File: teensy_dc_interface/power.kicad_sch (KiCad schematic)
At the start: 51 parts, among them U3 AP65211A, U4 AP62200TWU-7, U9 AP65211A

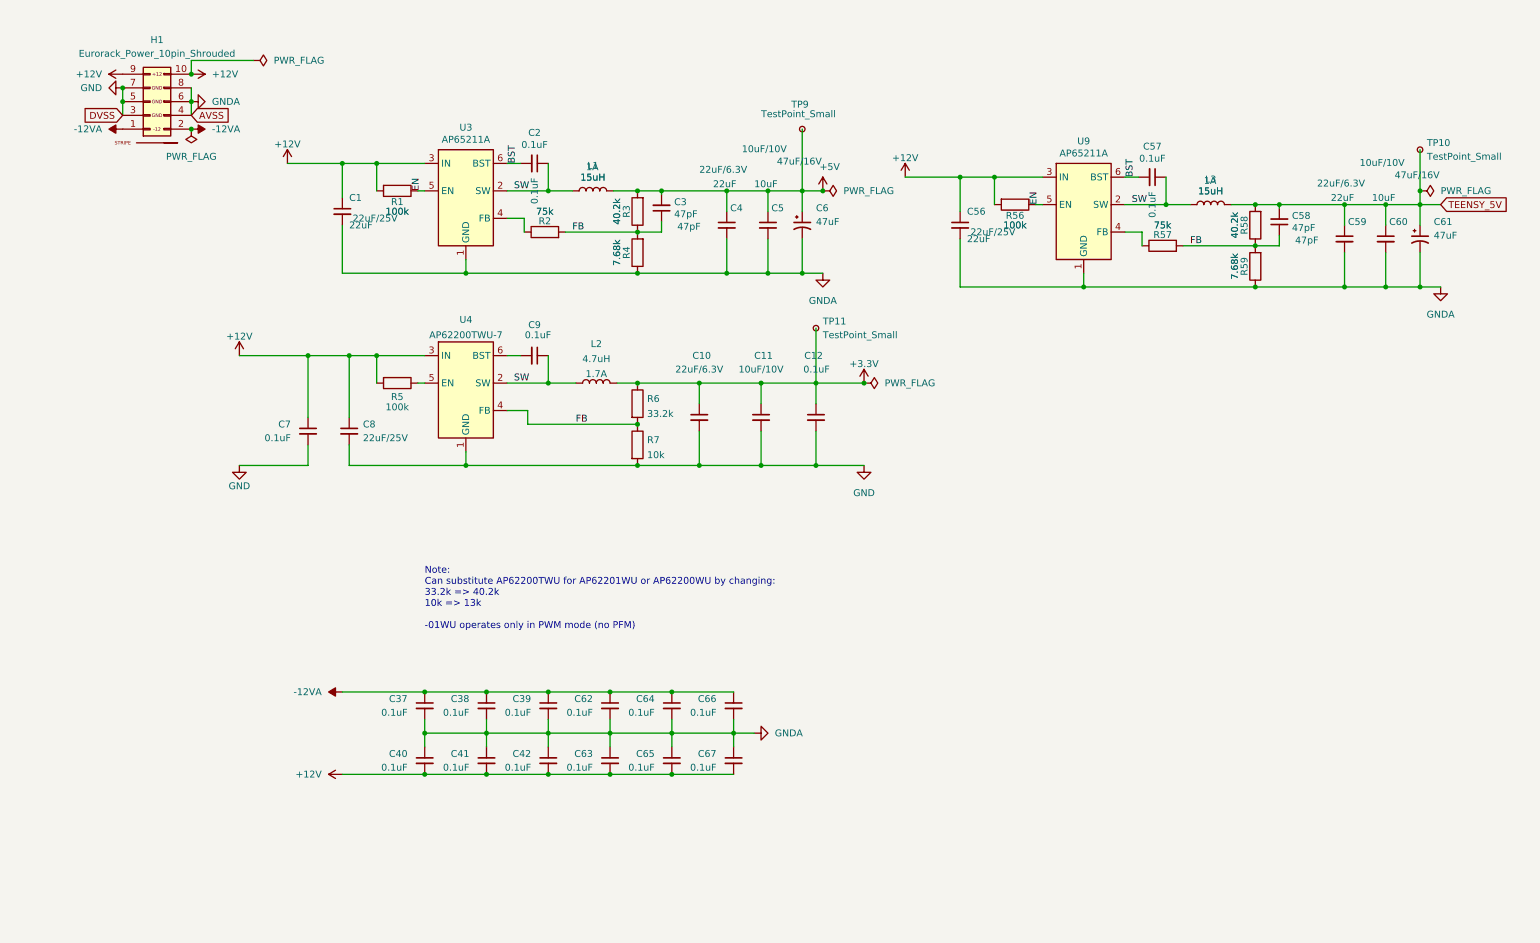
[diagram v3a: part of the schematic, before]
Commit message: Added layout for power regulators
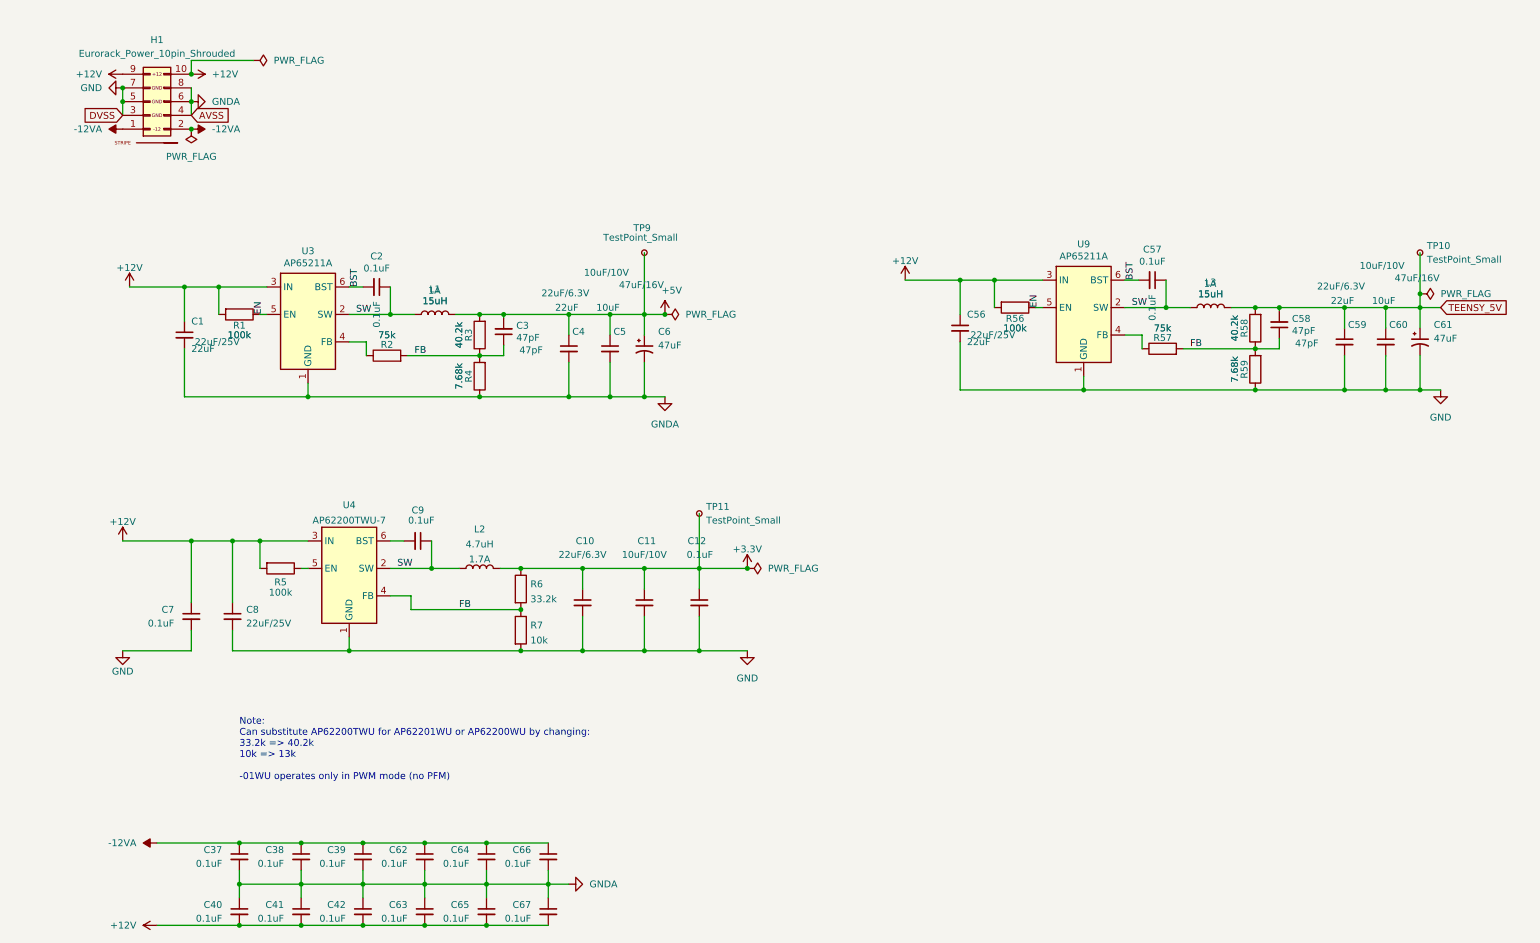
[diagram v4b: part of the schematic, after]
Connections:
- net GND: now also C56.2, C59.2, C60.2, C61.2, R59.1, U9.1 (GND)
- net GNDA: no longer C56.2, C59.2, C60.2, C61.2, R59.1, U9.1 (GND)
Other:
- moved on the sheet: C1, C10, C11, C12, C2, C3, C37, C38, C39, C4, C40, C41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

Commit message: Finished core electrical layout
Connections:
- net SW: no longer C2.1, C57.1, L1.1, L3.1, U3.2 (SW), U9.2 (SW)
- net BST: no longer names the net of C57.2, U9.6 (BST)
- net BST: no longer C2.2, U3.6 (BST)
- net EN: no longer names the net of R1.1, U3.5 (EN)
- net EN: no longer R56.1, U9.5 (EN)
- removed net FB: C3.1, C58.1, R2.2, R3.1, R4.2, R57.2, R58.1, R59.2, R6.2, R7.1, U4.4 (FB)
- new net: R6.2, R7.1, U4.4 (FB)
- new net: C57.1, L3.1, U9.2 (SW)
- new net: C3.1, R2.2, R3.1, R4.2
- new net: R56.1, U9.5 (EN)
- new net: C2.1, L1.1, U3.2 (SW)
- new net: C2.2, U3.6 (BST)
- new net: C58.1, R57.2, R58.1, R59.2
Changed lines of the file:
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@@
-	)
-	(label "SW"
-		(at 68.58 72.39 0)
-		(fields_autoplaced yes)
-		(effects
-			(font
-				(size 1.27 1.27)
-			)
-			(justify left bottom)
-		)
 	)
 	(label "SW"
@@
 		(fields_autoplaced yes)
 		(effects
-			(font
-				(size 1.27 1.27)
-			)
-			(justify left bottom)
-		)
-	)
-	(label "SW"
-		(at 212.09 71.12 0)
-		(fields_autoplaced yes)
-		(effects
-			(font
-				(size 1.27 1.27)
-			)
-			(justify left bottom)
-		)
-	)
-	(label "FB"
-		(at 79.375 80.01 0)
-		(fields_autoplaced yes)
-		(effects
-			(font
-				(size 1.27 1.27)
-			)
-			(justify left bottom)
-		)
-	)
-	(label "BST"
-		(at 212.725 66.04 90)
-		(fields_autoplaced yes)
-		(effects
-			(font
-				(size 1.27 1.27)
-			)
-			(justify left bottom)
-		)
-	)
-	(label "FB"
-		(at 222.885 78.74 0)
-		(fields_autoplaced yes)
-		(effects
-			(font
-				(size 1.27 1.27)
-			)
-			(justify left bottom)
-		)
-	)
-	(label "BST"
-		(at 69.215 67.31 90)
-		(fields_autoplaced yes)
-		(effects
-			(font
-				(size 1.27 1.27)
-			)
-			(justify left bottom)
-		)
-	)
-	(label "FB"
-		(at 87.63 127 0)
-		(fields_autoplaced yes)
-		(effects
-			(font
-				(size 1.27 1.27)
-			)
-			(justify left bottom)
-		)
-	)
-	(label "EN"
-		(at 194.945 71.12 90)
-		(fields_autoplaced yes)
-		(effects
-			(font
-				(size 1.27 1.27)
-			)
-			(justify left bottom)
-		)
-	)
-	(label "EN"
-		(at 51.435 72.39 90)
-		(fields_autoplaced yes)
-		(effects

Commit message: sizing, remove SW label
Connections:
- net SW: no longer names the net of C9.1, L2.1, U4.2 (SW)
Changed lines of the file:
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@@
 		)
 	)
-	(label "SW"
-		(at 76.2 119.38 0)
-		(fields_autoplaced yes)
-		(effects
-			(font
-				(size 1.27 1.27)
-			)
-			(justify left bottom)
-		)
-	)
 	(global_label "TEENSY_5V"
 		(shape input)
@@
 		)
 		(property "Display" "15uH"
-			(at 226.695 68.58 90)
+			(at 227.33 67.31 90)
 			(effects
 				(font
@@
 		)
 		(property "Display 2" "1A"
-			(at 226.5934 66.7004 90)
+			(at 226.822 64.262 90)
 			(effects
 				(font
@@
 		)
 		(property "Display" "47uF/16V"
-			(at 260.731 65.659 0)
+			(at 265.176 64.77 0)
 			(effects
 				(font
@@
 		)
 		(property "Display" "10uF/10V"
-			(at 254.254 63.373 0)
+			(at 254.254 64.008 0)
 			(effects
 				(font

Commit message: Generated gerbers for boards
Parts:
- removed C1, C56: 22uF, 4ms_Capacitor:C_0805, symbol 4ms_Capacitor:22uF_0805_25V
- removed C10: 22uF_0805_6.3V, 4ms_Capacitor:C_0805, symbol 4ms_Capacitor:22uF_0805_6.3V
- removed C11: 10uF_0603_10V, 4ms_Capacitor:C_0603, symbol 4ms_Capacitor:10uF_0603_10V
- removed C12, C7, C9: 0.1uF_0603_16V, 4ms_Capacitor:C_0603, symbol 4ms_Capacitor:0.1uF_0603_16V
- removed C2, C57: 0.1uF, 4ms_Capacitor:C_0603, symbol 4ms_Capacitor:0.1uF_0603_16V
- removed C3, C58: 47pF, 4ms_Capacitor:C_0603, symbol 4ms_Capacitor:47pF_0603_50V
- removed C4, C59: 22uF, 4ms_Capacitor:C_0603, symbol 4ms_Capacitor:22uF_0603_6.3V
- removed C5, C60: 10uF, 4ms_Capacitor:C_0603, symbol 4ms_Capacitor:10uF_0603_10V
- removed C6, C61: 47uF, 4ms_Capacitor:CP_Elec_5x5.3, symbol 4ms_Capacitor:47uF_5x5.3_16V
- removed C8: 22uF_0805_25V, 4ms_Capacitor:C_0805, symbol 4ms_Capacitor:22uF_0805_25V
- removed L1, L3: 15uH, 4ms_Inductor:COIL_5040, symbol 4ms_Inductor:15uH_1A_5040
- removed L2: 4.7uH_1.2A_40xx, Inductor_SMD:L_Taiyo-Yuden_NR-40xx, symbol 4ms_Inductor:4.7uH_1.2A_40xx
- removed R1, R56: 100k, 4ms_Resistor:R_0603, symbol 4ms_Resistor_0603:100k_0603
- removed R2, R57: 75k, 4ms_Resistor:R_0603, symbol 4ms_Resistor:75k_0603
- removed R3, R58: 40.2k, 4ms_Resistor:R_0603, symbol 4ms_Resistor:40.2k_0603
- removed R4, R59: 7.68k, 4ms_Resistor:R_0603, symbol 4ms_Resistor:7.68k_0603
- removed R5: 100k_0603, 4ms_Resistor:R_0603, symbol 4ms_Resistor:100k_0603
- removed R6: 33.2k_0603, 4ms_Resistor:R_0603, symbol 4ms_Resistor:33.2k_0603
- removed R7: 10k_0603, 4ms_Resistor:R_0603, symbol 4ms_Resistor:10k_0603
- removed U3, U9: AP65211A, 4ms_Package_SOT:TSOT-23-6, symbol 4ms_IC:AP65211AWU-7
- removed U4: AP62200TWU-7, 4ms_Package_SOT:TSOT-23-6, symbol 4ms_IC:AP62200TWU-7
- added C1, C3, C5: 10uF_0805_25V, 4ms_Capacitor:C_0805, symbol 4ms_Capacitor:10uF_0805_25V
- added C2, C4, C6: 10uF_0603_10V, 4ms_Capacitor:C_0603, symbol 4ms_Capacitor:10uF_0603_10V
- added U10, U4: NCP1117-5.0_SOT223, Package_TO_SOT_SMD:SOT-223-3_TabPin2, symbol Regulator_Linear:NCP1117-5.0_SOT223
- added U3: NCP1117-3.3_SOT223, Package_TO_SOT_SMD:SOT-223-3_TabPin2, symbol Regulator_Linear:NCP1117-3.3_SOT223
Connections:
- net +12V: now also C1.1, C3.1, C5.1, U10.3 (VI), U3.3 (VI), U4.3 (VI)
- net +3.3V: now also C6.1, U3.2 (VO)
- net +5V: now also C2.1, U10.2 (VO)
- net GND: now also C3.2, C4.2, C5.2, C6.2, U3.1 (GND), U4.1 (GND)
- net GNDA: now also C1.2, C2.2, U10.1 (GND)
- net TEENSY_5V: now also C4.1, U4.2 (VO)
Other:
- moved on the sheet: TP10, TP9
